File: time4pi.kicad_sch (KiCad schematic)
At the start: 10 parts, among them J1 Raspberry_Pi_2_3, J2 Conn_02x03_Odd_Even, U3 ADF4158, U4 AB0805

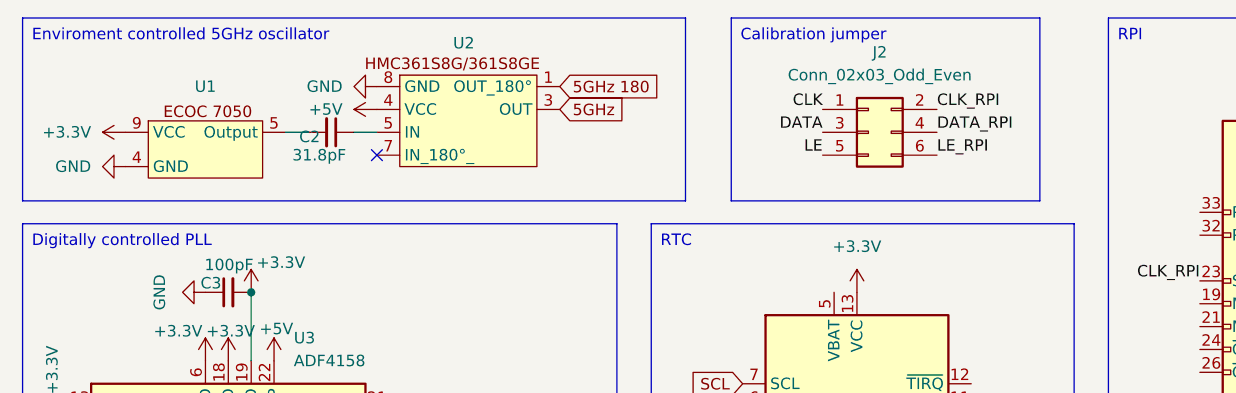
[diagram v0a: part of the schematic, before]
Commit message: fix: symbol values
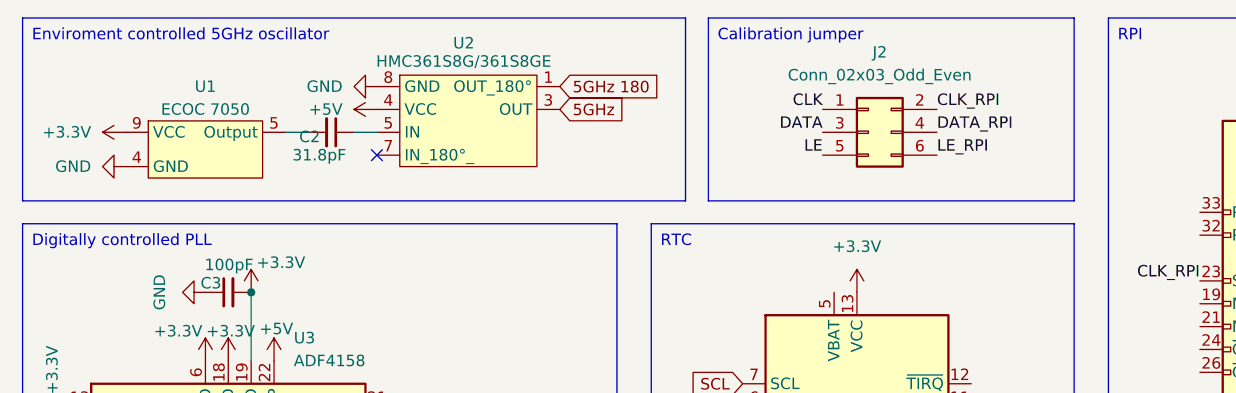
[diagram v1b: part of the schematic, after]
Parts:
- U1: value ~ -> ECOC 7050
- U2: value ~ -> HMC361S8G/361S8GE
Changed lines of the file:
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@@
 	(text_box "Calibration jumper"
 		(exclude_from_sim no)
-		(at 95.25 16.51 0)
-		(size 34.29 20.32)
+		(at 92.71 16.51 0)
+		(size 40.64 20.32)
 		(stroke
 			(width 0)
@@
 			)
 		)
-		(property "Value" "~"
-			(at 64.262 19.05 0)
+		(property "Value" "HMC361S8G/361S8GE"
+			(at 65.532 21.336 0)
 			(effects
 				(font
@@
 			)
 		)
-		(property "Value" "~"
+		(property "Value" "ECOC 7050"
 			(at 36.83 26.67 0)
 			(effects

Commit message: feat: finished v0.1
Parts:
- added C4: 100pF, Capacitor_SMD:C_0201_0603Metric, symbol Device:C_Small
- added J3, J4: Conn_Coaxial_Small, Connector_Coaxial:SMA_Amphenol_901-143_Horizontal, symbol Connector:Conn_Coaxial_Small
- added J5: RFShield_OnePiece, symbol Device:RFShield_OnePiece
- added Q3, Q4: BFR92, Package_TO_SOT_SMD:SOT-323_SC-70, symbol Transistor_BJT:BFR92
- added R2: 10k, Resistor_SMD:R_0201_0603Metric, symbol Device:R_Small
- J1: footprint ice4pi:PinSocket_2x20_P2.54mm_Vertical_1_04mm -> Module:Raspberry_Pi_Zero_Socketed_THT_FaceDown_MountingHoles
- J2: footprint (none) -> Connector_PinHeader_1.00mm:PinHeader_2x03_P1.00mm_Vertical
- U1: footprint (none) -> LSI:ECOC 7050
- U2: footprint (none) -> LSI:HMC361S8G361S8GE
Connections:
- net +5V: now also Q3.3 (C), Q4.3 (C)
- net CLK: now also J2.5 (Pin_5); no longer J2.1 (Pin_1)
- net CLK_RPI: now also J2.6 (Pin_6); no longer J2.2 (Pin_2)
- net Fout: now also Q4.1 (B), R2.2
- net GND: now also C4.2, J3.2 (Ext), J4.2 (Ext), J5.1 (Shield), R2.1
- net LE: now also J2.1 (Pin_1); no longer J2.5 (Pin_5)
- net LE_RPI: now also J2.2 (Pin_2); no longer J2.6 (Pin_6)
- net at U2.7 (IN_180°_): now also C4.1
- net 5GHz renamed 5GHz_P
- net 5GHz_P: now also U2.1 (OUT_180°), Q3.1 (B); no longer U2.3 (OUT)
- net 5GHz 180 renamed 5GHz_N
- net 5GHz_N: now also U2.3 (OUT); no longer U2.1 (OUT_180°)
- new net: J3.1 (In), Q3.2 (E)
- new net: J4.1 (In), Q4.2 (E)
- no-connect marks 7 -> 37

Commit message: feat: more caps
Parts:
- added C10: 10uf, Capacitor_SMD:CP_Elec_4x3, symbol Device:C_Polarized
- added C11: 1000pF, Capacitor_SMD:C_0201_0603Metric, symbol Device:C_Small
- added C5: 10uf, Capacitor_SMD:C_0201_0603Metric, symbol Device:C
- added C6: 0.1uf, Capacitor_SMD:C_0201_0603Metric, symbol Device:C
- added C7: 15pf, Capacitor_SMD:C_0201_0603Metric, symbol Device:C
- added C8, C9: 100pf, Capacitor_SMD:C_0201_0603Metric, symbol Device:C
- C2: value 31.8pF -> 100pF
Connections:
- net +3.3V: now also C5.2, C6.2
- net +5V: now also C10.1, C11.2
- net 5GHz_N: now also C8.1; no longer U2.3 (OUT)
- net 5GHz_P: now also C9.1; no longer U2.1 (OUT_180°)
- net GND: now also C10.2, C11.1, C5.1, C6.1, C7.2
- net at C2.2, U1.5 (Output): now also C7.1
- new net: C8.2, U2.3 (OUT)
- new net: C9.2, U2.1 (OUT_180°)
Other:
- moved on the sheet: C4, J1, J2, U2

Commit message: feat: added ice40fpga
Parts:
- removed U4: AB0805, Package_DFN_QFN:VQFN-16-1EP_3x3mm_P0.5mm_EP1.8x1.8mm, symbol Timer_RTC:AB0805
- added C12, C13: 10nF, Capacitor_SMD:C_0201_0603Metric, symbol Device:C_Small
- added C14, C16, C18: 1uF, Capacitor_SMD:C_0201_0603Metric, symbol Device:C_Small
- added C15, C17, C19, C20, C23, C25: 0.1uF, Capacitor_SMD:C_0201_0603Metric, symbol Device:C_Small
- added C21, C22, C24: 10uF, Capacitor_SMD:C_0201_0603Metric, symbol Device:C_Small
- added R3: 33 Ohm, Resistor_SMD:R_0201_0603Metric, symbol Device:R_Small
- added R4, R5: 100k, Resistor_SMD:R_0201_0603Metric, symbol Device:R_Small
- added U4: LT1761-1.2, Package_TO_SOT_SMD:TSOT-23-5, symbol Regulator_Linear:LT1761-1.2
- added U5: LT1761-2.5, Package_TO_SOT_SMD:TSOT-23-5, symbol Regulator_Linear:LT1761-2.5
- added U6: ICE40UP5K-SG48ITR, Package_DFN_QFN:QFN-48-1EP_7x7mm_P0.5mm_EP5.6x5.6mm, symbol FPGA_Lattice:ICE40UP5K-SG48ITR
- C10: footprint Capacitor_SMD:CP_Elec_4x3 -> Capacitor_Tantalum_SMD:CP_EIA-3216-10_Kemet-I
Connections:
- net +3.3V: now also C20.2, C21.2, C22.2, C23.2, C24.2, C25.2, R4.2, R5.2, U4.1 (VIN), U5.1 (VIN), U6.1 (VCCIO_2), U6.22 (SPI_VCCIO1), U6.33 (VCCIO_0)
- net CLK: no longer U3.14 (CLK)
- net CLK_RPI: no longer J1.23 (SCLK0/GPIO11)
- net DATA: no longer U3.15 (DATA)
- net DATA_RPI: no longer J1.13 (GPIO27)
- net Fout: now also R3.1
- net GND: now also C12.1, C13.1, C14.1, C15.1, C16.1, C17.1, C18.1, C19.1, C20.1, C21.1, C22.1, C23.1, C24.1, C25.1, U4.2 (GND), U5.2 (GND), U6.49 (GND)
- net LE: no longer U3.16 (LE)
- net LE_RPI: no longer J1.10 (GPIO15/RXD)
- net SPI_SI: now reaches J1.19 (MOSI0/GPIO10)
- net SPI_SI: now also U6.17 (IOB_33b_SPI_SI)
- net SPI_SO: now reaches J1.21 (MISO0/GPIO9)
- net SPI_SO: now also U6.14 (IOB_32a_SPI_SO)
- net SPI_SS: now reaches J1.24 (~{CE0}/GPIO8)
- net SPI_SS: now also U6.16 (IOB_35b_SPI_SS)
- net SCL: no longer names the net of J1.5 (SCL/GPIO3)
- net SDA: no longer names the net of J1.3 (SDA/GPIO2)
- new net: C13.2, U5.4 (BYP)
- new net: R4.1, U4.3 (~{SHDN})
- new net: R5.1, U5.3 (~{SHDN})
- new net: R3.2, U6.44 (IOB_3b_G6)
- new net: C12.2, U4.4 (BYP)
- new net +1V2: C14.2, C15.2, C16.2, C17.2, U4.5 (VOUT), U6.29 (VCCPLL), U6.30 (VCC), U6.5 (VCC)
- new net +2V5: C18.2, C19.2, U5.5 (VOUT), U6.24 (VPP_2V5)
- new net CRESET: J1.13 (GPIO27), U6.18 (IOB_31b)
- new net PLL_CLK: U3.14 (CLK), U6.19 (IOB_29b)
- new net PLL_DATA: U3.15 (DATA), U6.13 (IOB_24a)
- new net PLL_LE: U3.16 (LE), U6.21 (IOB_23b)
- new net SPI_SCK: J1.23 (SCLK0/GPIO11), U6.15 (IOB_34a_SPI_SCK)
- no-connect marks 37 -> 28

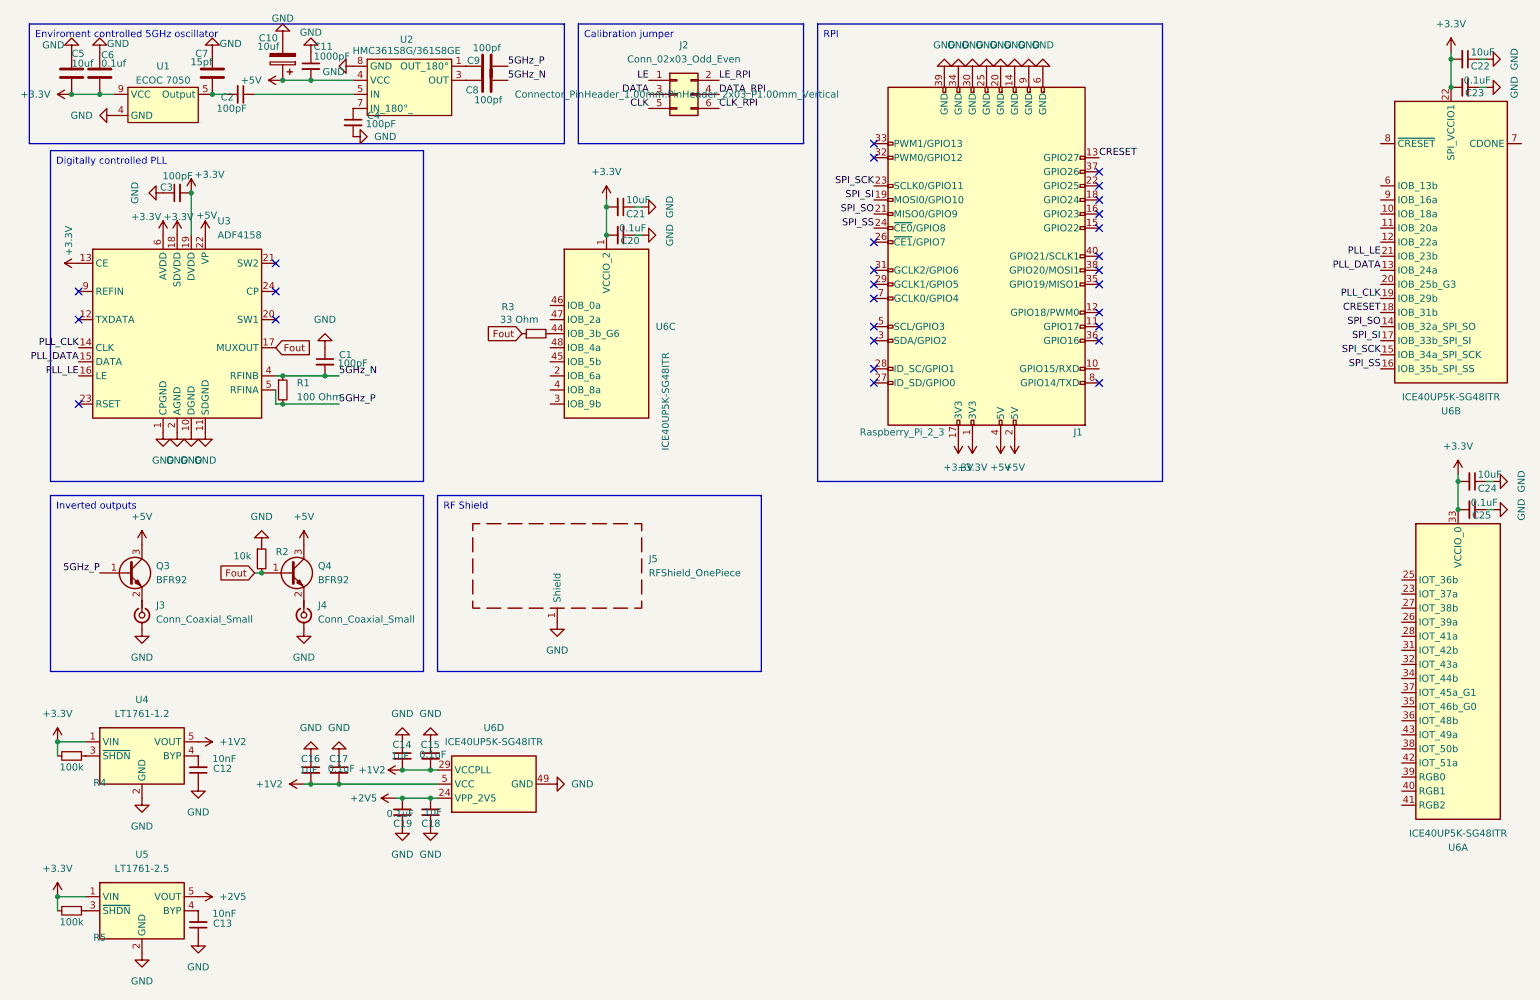
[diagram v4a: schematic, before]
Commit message: feat: added stitched vias
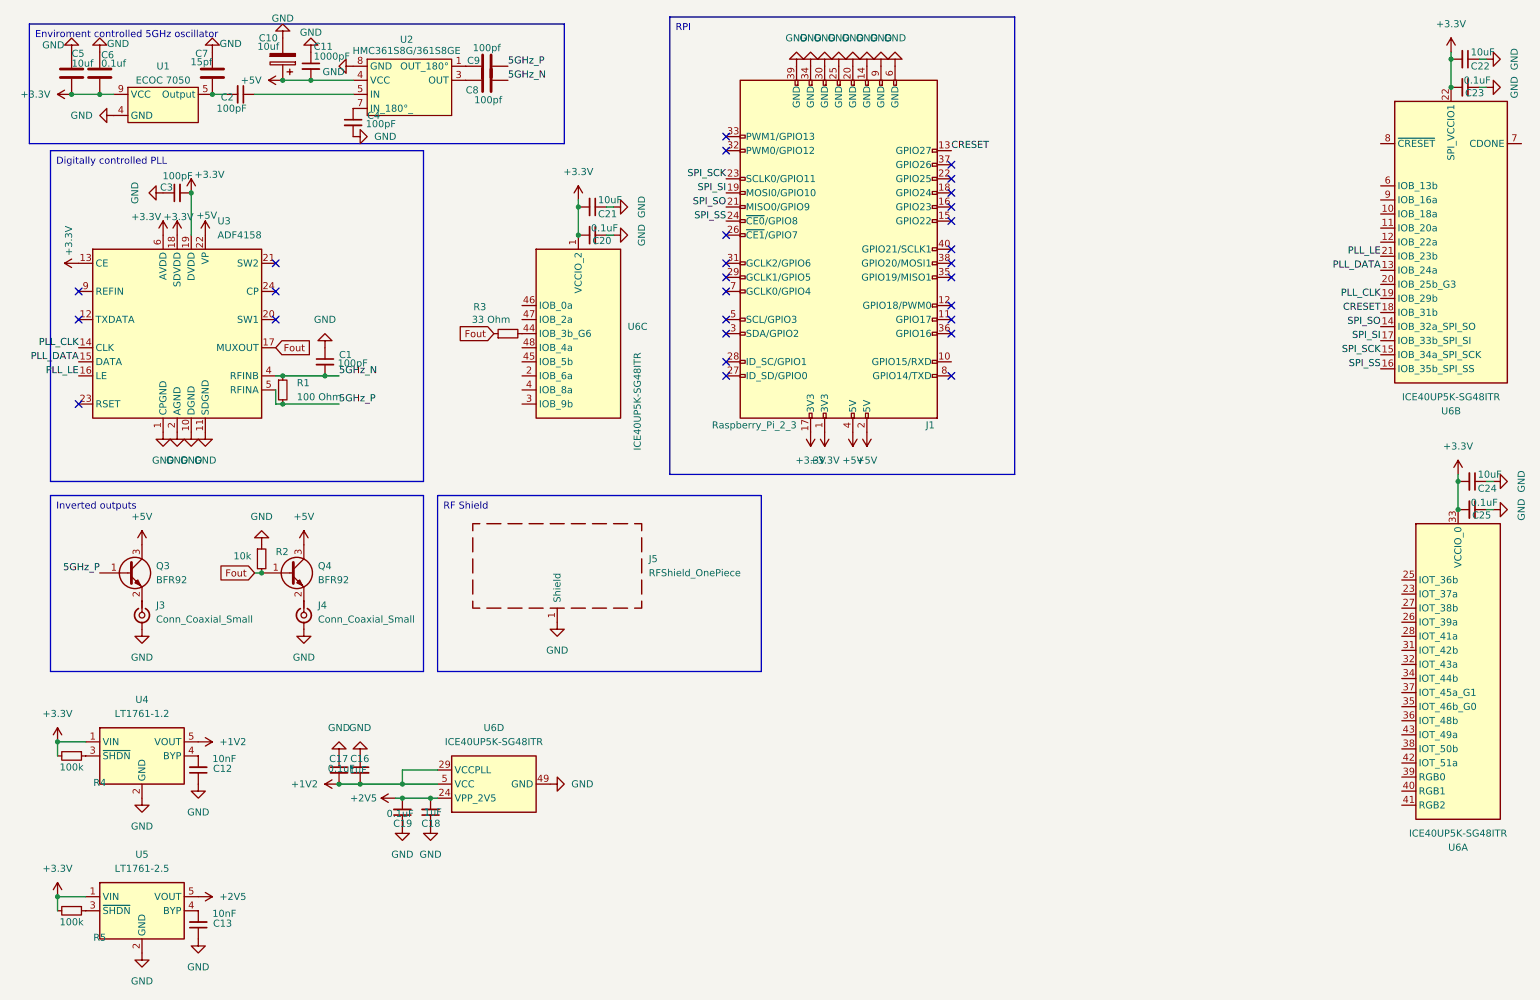
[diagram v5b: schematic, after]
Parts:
- removed C14: 1uF, Capacitor_SMD:C_0201_0603Metric, symbol Device:C_Small
- removed C15: 0.1uF, Capacitor_SMD:C_0201_0603Metric, symbol Device:C_Small
- removed J2: Conn_02x03_Odd_Even, Connector_PinHeader_1.00mm:PinHeader_2x03_P1.00mm_Vertical, symbol Connector_Generic:Conn_02x03_Odd_Even
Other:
- moved on the sheet: C16, C20, C21, J1, R3, U6C
